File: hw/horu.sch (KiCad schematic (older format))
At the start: 30 parts, among them P101 CONN_01X30_2SHIELD, P102 CONN_02X05, U101 KL25P80M48SF0, Y101 8MHz

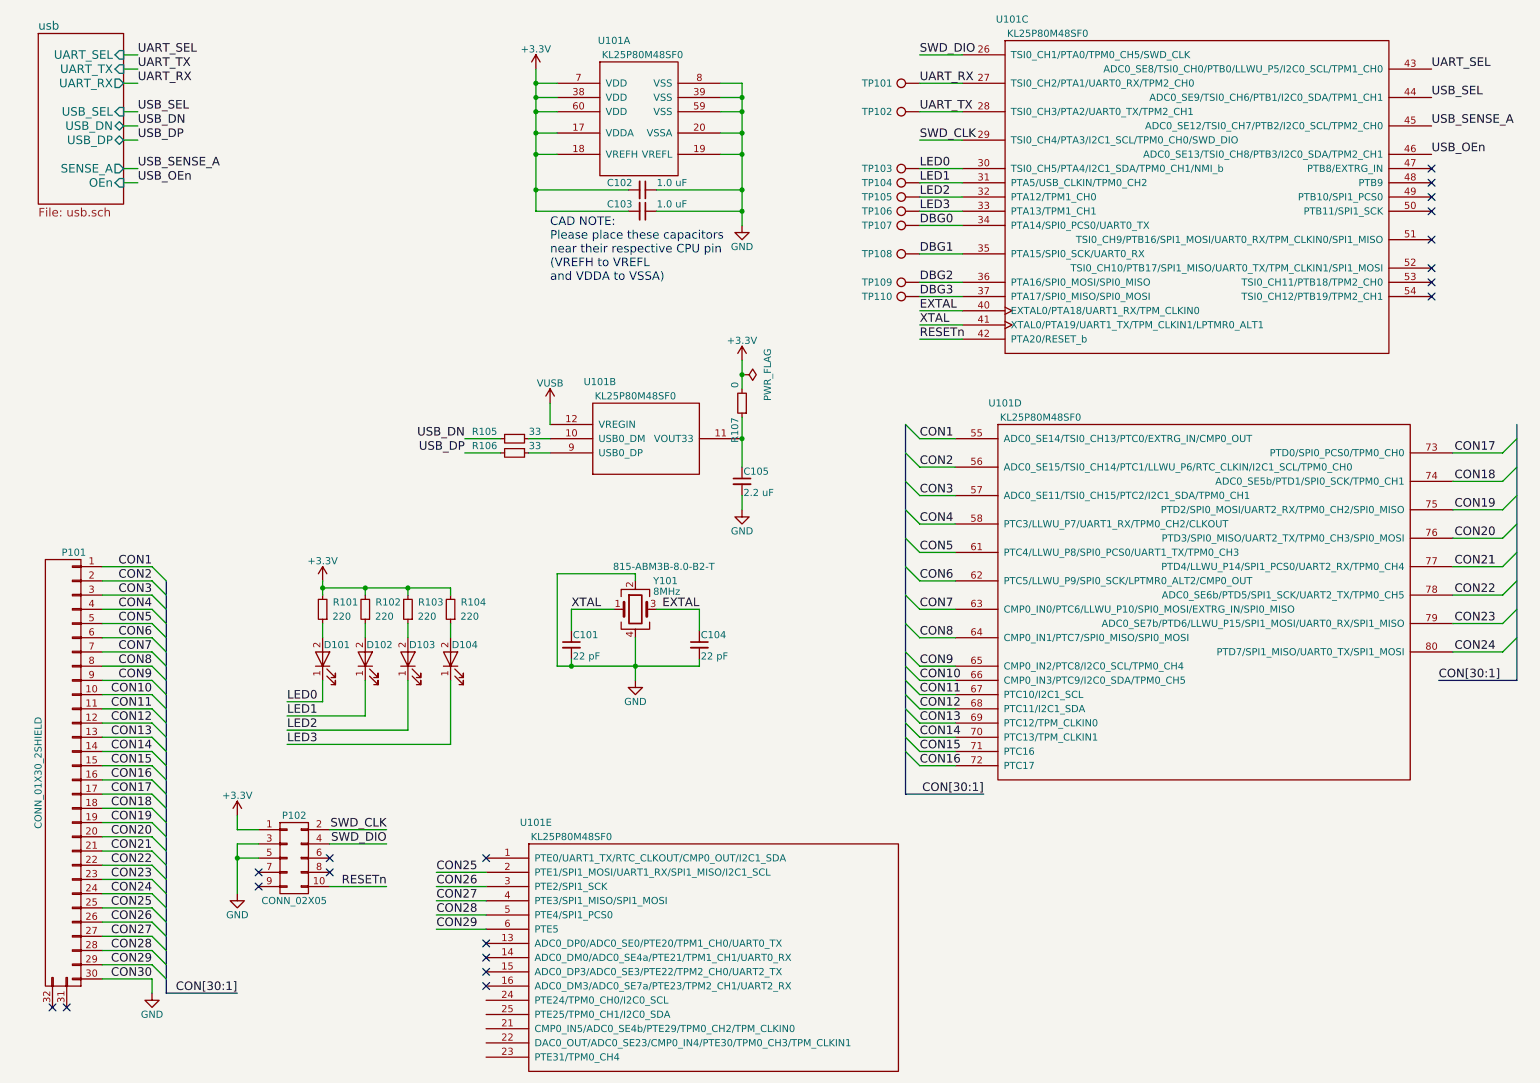
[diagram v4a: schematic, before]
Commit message: Update to v0.1 release
* Fall back to simple mUSB-B (connector + pigtail supported)
* First pass at layout
* Added missing pull-up to RESETn
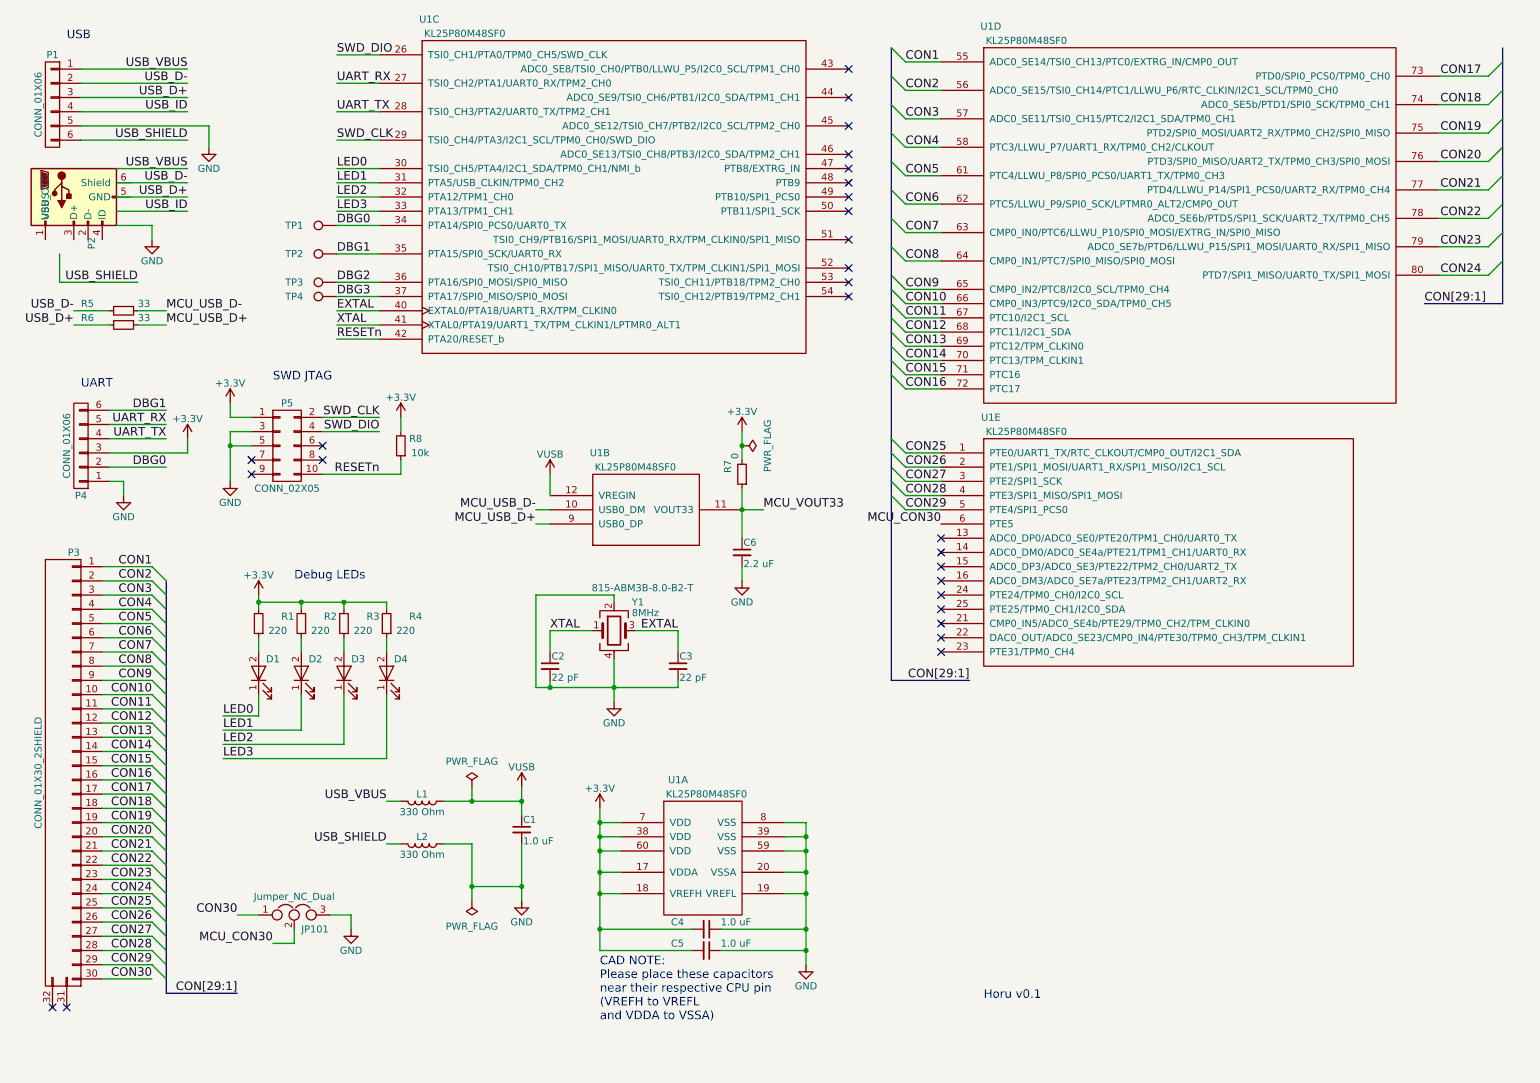
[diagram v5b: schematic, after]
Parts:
- removed TP101, TP102, TP103, TP104, TP105, TP106: TEST_1P, Measurement_Points:Measurement_Point_Round-TH_Small, symbol TEST_1P
- added C1: 1.0 uF, Resistors_SMD:R_0603_HandSoldering, symbol C_Small
- added JP101: Jumper_NC_Dual, Connectors:GS3, symbol Jumper_NC_Dual
- added L1, L2: 330 Ohm, Resistors_SMD:R_0603_HandSoldering, symbol L
- added P1, P4: CONN_01X06, horu:PINHEAD1-6, symbol CONN_01X06
- added P2: USB_OTG, Connectors:USB_Micro-B, symbol USB_OTG
- added R8: 10k, Resistors_SMD:R_0603_HandSoldering, symbol R_Small
- U1: renamed from U101; footprint Housings_QFP:LQFP-80_12x12mm_Pitch0.5mm -> horu:LQFP-80_12x12mm_Pitch0.5mm
- renumbered C101 to C2, C104 to C3, C102 to C4, C103 to C5, C105 to C6, D101 to D1, D102 to D2, D103 to D3, D104 to D4, P101 to P3, P102 to P5, R101 to R1, R102 to R2, R103 to R3, R104 to R4, R105 to R5, R106 to R6, R107 to R7, TP107 to TP1, TP108 to TP2, TP109 to TP3, TP110 to TP4, Y101 to Y1
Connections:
- net +3V3_SDA: now also P4.3 (P3), R8.2
- net CON25: now also U1.1 (PTE0/UART1_TX/RTC_CLKOUT/CMP0_OUT/I2C1_SDA); no longer U1.2 (PTE1/SPI1_MOSI/UART1_RX/SPI1_MISO/I2C1_SCL)
- net CON26: now also U1.2 (PTE1/SPI1_MOSI/UART1_RX/SPI1_MISO/I2C1_SCL); no longer U1.3 (PTE2/SPI1_SCK)
- net CON27: now also U1.3 (PTE2/SPI1_SCK); no longer U1.4 (PTE3/SPI1_MISO/SPI1_MOSI)
- net CON28: now also U1.4 (PTE3/SPI1_MISO/SPI1_MOSI); no longer U1.5 (PTE4/SPI1_PCS0)
- net CON29: now also U1.5 (PTE4/SPI1_PCS0); no longer U1.6 (PTE5)
- net DBG0: now also P4.2 (P2)
- net DBG1: now also P4.6 (P6)
- net GND: now also C1.2, JP101.3, L2.1, P1.5 (P5), P4.1 (P1); no longer P3.30 (P30)
- net RESETn: now also R8.1
- net UART_RX: now also P4.5 (P5)
- net UART_TX: now also P4.4 (P4)
- net VUSB: now also C1.1, L1.1
- net MCU_USB_D-: now reaches R5.1, U1.10 (USB0_DM)
- net MCU_VOUT33: now reaches C6.1, R7.1, U1.11 (VOUT33)
- net MCU_USB_D+: now reaches R6.1, U1.9 (USB0_DP)
- net UART_SEL: no longer names the net of U1.43 (ADC0_SE8/TSI0_CH0/PTB0/LLWU_P5/I2C0_SCL/TPM1_CH0)
- net USB_DN renamed USB_D-
- net USB_D-: now also P1.2 (P2)
- net USB_DP renamed USB_D+
- net USB_D+: now also P1.3 (P3)
- net USB_OEn: no longer names the net of U1.46 (ADC0_SE13/TSI0_CH8/PTB3/I2C0_SDA/TPM2_CH1)
- net USB_SEL: no longer names the net of U1.44 (ADC0_SE9/TSI0_CH6/PTB1/I2C0_SDA/TPM1_CH1)
- net USB_SENSE_A: no longer names the net of U1.45 (ADC0_SE12/TSI0_CH7/PTB2/I2C0_SCL/TPM2_CH0)
- new net CON30: JP101.1, P3.30 (P30)
- new net MCU_CON30: JP101.2, U1.6 (PTE5)
- new net USB_ID: P1.4 (P4)
- new net USB_SHIELD: L2.2, P1.6 (P6)
- new net USB_VBUS: L1.2, P1.1 (P1)
- no-connect marks 19 -> 27
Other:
- note added: "Debug LEDs"
- note added: "Horu v0.1"
- note added: "SWD JTAG"
- note added: "UART"
- note added: "USB"
- moved on the sheet: C2, C3, C4, C5, C6, D1, D2, D3, D4, P5, R1, R2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

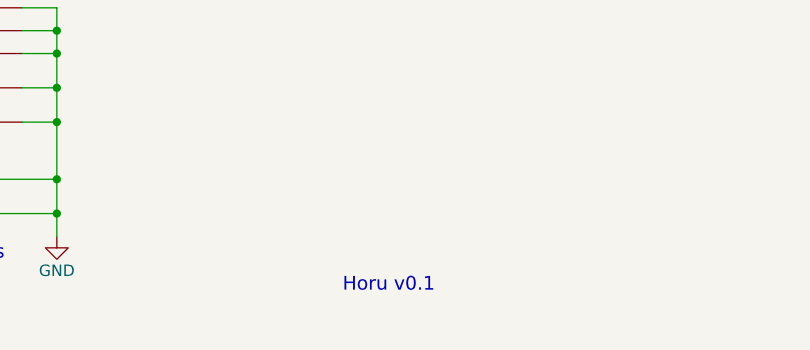
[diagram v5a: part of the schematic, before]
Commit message: Changed to copper pour for each layer
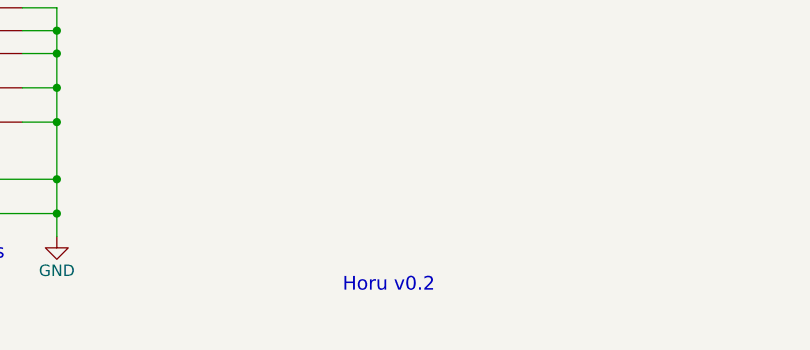
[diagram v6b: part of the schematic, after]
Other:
- note added: "Horu v0.2"
- note removed: "Horu v0.1"
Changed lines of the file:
@@
 	2500 7100 2350 7100
 Text Notes 7350 7500 0    60   ~ 0
-Horu v0.1
+Horu v0.2
 $EndSCHEMATC

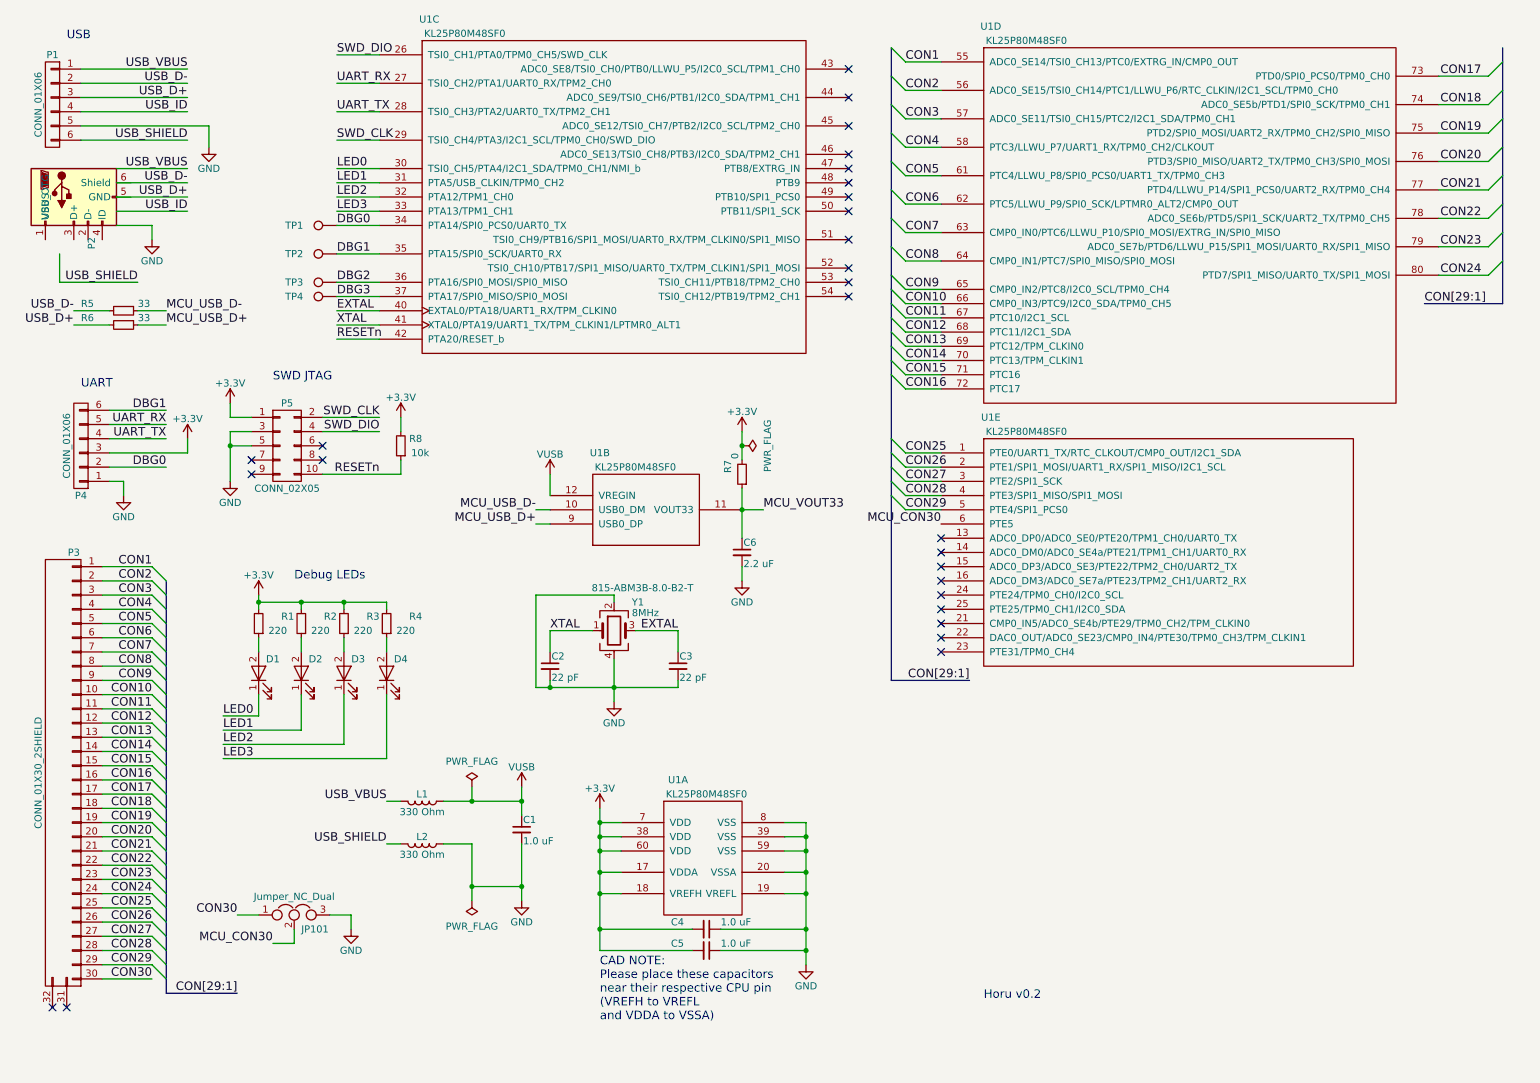
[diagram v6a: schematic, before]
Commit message: Update schematic and prepare for release
* Update rev to v1.0
* Update USB_OTG symbol
* Add missing USB ESD diodes
* Fill in manf# for all parts
* Export BOM using kicost
* Fill ground on bottom layer
* Replace traces on inner 2 with properly placed vias to allow fill to connect everything
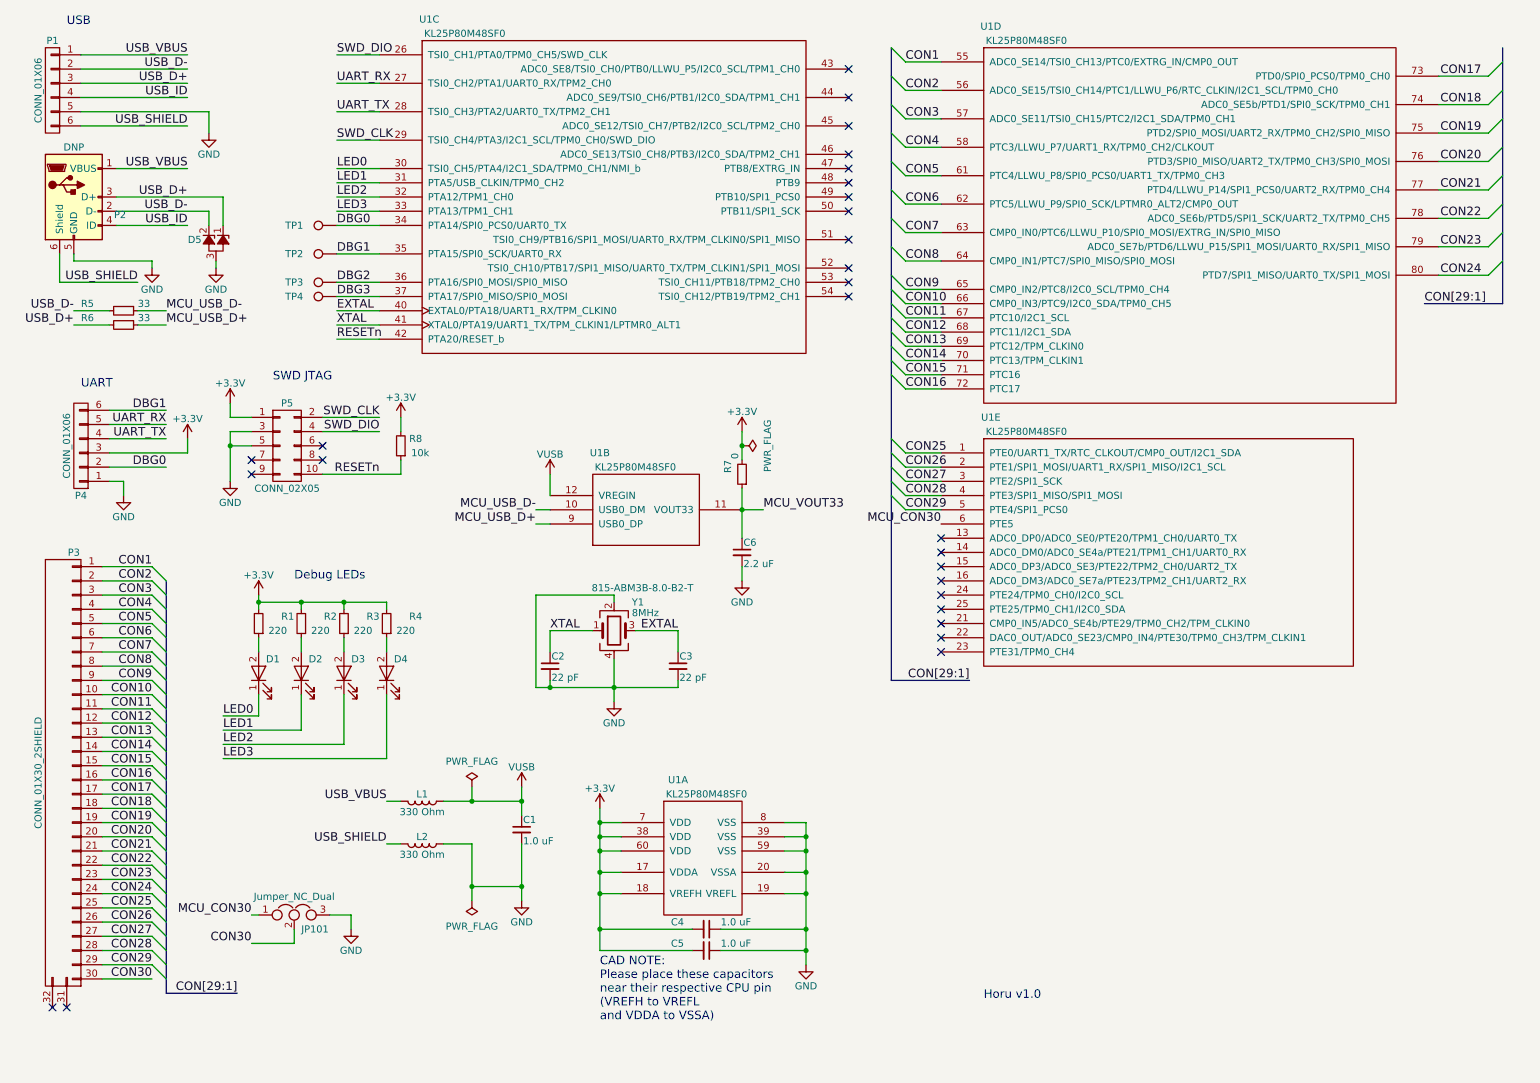
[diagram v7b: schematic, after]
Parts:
- added D5: D_Zener_x2_ACom_KKA, TO_SOT_Packages_SMD:SOT-23, symbol D_Zener_x2_ACom_KKA
- C1, C4, C5: DstPart (none) -> 81-GRM39R105K16; manf# (none) -> GRM188R61C105KA93D
- C2, C3: DstPart (none) -> 81-GRM39C220J50; manf# (none) -> GRM1885C1H220JA01D
- C6: DstPart (none) -> 81-GRM188R61C225KE15; manf# (none) -> GRM188R61C225KE15D
- D1, D2, D3, D4: DstPart (none) -> 720-LGQ396A3964; manf# (none) -> LG Q396-PS-35
- L1, L2: DstPart (none) -> 81-BLM18SG331TN1D; manf# (none) -> BLM18SG331TN1D
- P1, P4: DstPart (none) -> 571-4-103327-6; manf# (none) -> 4-103327-6
- P2: value USB_OTG -> DNP
- P3: DstPart (none) -> 538-52271-3079; manf# (none) -> 52271-3079
- P5: DstPart (none) -> 649-202112100010C4LF; manf# (none) -> 20021121-00010C4LF
- R1, R2, R3, R4: DstPart (none) -> 667-ERJ-3GEYJ221V; manf# (none) -> ERJ-3GEYJ221V
- R5, R6: DstPart (none) -> 667-ERJ-3GEYJ330V; manf# (none) -> ERJ-3GEYJ330V
- R7: DstPart (none) -> 667-ERJ-3GEY0R00V; manf# (none) -> ERJ-3GEY0R00V
- R8: DstPart (none) -> 667-ERJ-3GEYJ103V; manf# (none) -> ERJ-3GEYJ103V
- U1: DstPart (none) -> 841-MKL25Z128VLK4; manf# (none) -> MKL25Z128VLK4
- U1: manf# (none) -> MKL25Z128VLK4
- Y1: DstPart (none) -> 815-ABM3B-8.0-B2-T; manf# (none) -> ABM3B-8.000MHZ-B2-T
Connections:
- net CON30: now also JP101.2; no longer JP101.1
- net GND: now also P2.5 (GND), D5.3 (A)
- net MCU_CON30: now also JP101.1; no longer JP101.2
- net USB_D+: now also P2.3 (D+), D5.1 (K)
- net USB_D-: now also P2.2 (D-), D5.2 (K)
- net USB_ID: now also P2.4 (ID)
- net USB_SHIELD: now also P2.6 (Shield)
- net USB_VBUS: now also P2.1 (VBUS)
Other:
- note added: "Horu v1.0"
- note removed: "Horu v0.2"
- moved on the sheet: P1

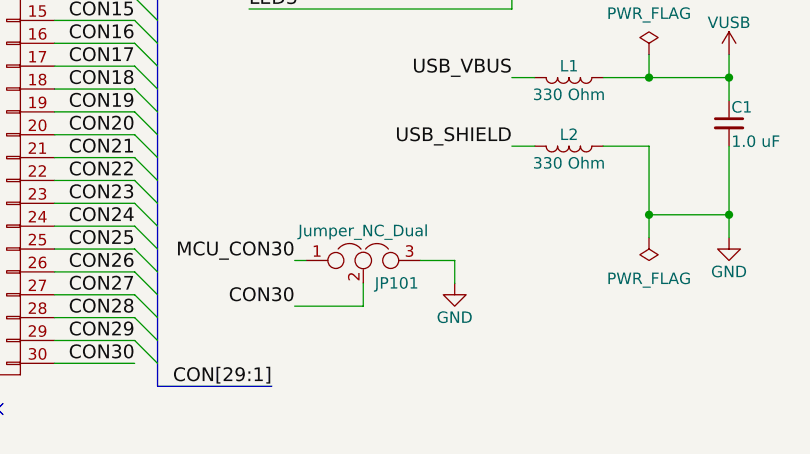
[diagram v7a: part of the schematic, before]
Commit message: Update design
* Fix JP101 -> JP1
* Update USB_OTG -> DNP
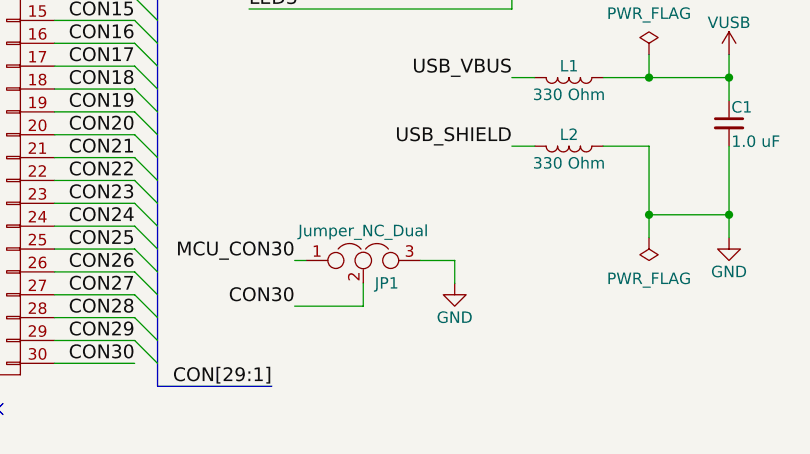
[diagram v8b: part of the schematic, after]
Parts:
- renumbered JP101 to JP1
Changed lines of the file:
@@
 	3250 3500 3250 3400
 $Comp
-L Jumper_NC_Dual JP101
+L Jumper_NC_Dual JP1
 U 1 1 58B39070
 P 2500 6900
-F 0 "JP101" H 2550 6800 50  0000 L CNN
+F 0 "JP1" H 2550 6800 50  0000 L CNN
 F 1 "Jumper_NC_Dual" H 2500 7000 50  0000 C BNN
 F 2 "Connectors:GS3" H 2500 6900 50  0001 C CNN
